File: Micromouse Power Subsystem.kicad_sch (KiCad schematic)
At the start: 3 parts, among them J2 Conn_02x16_Odd_Even, U1 INA219AxD

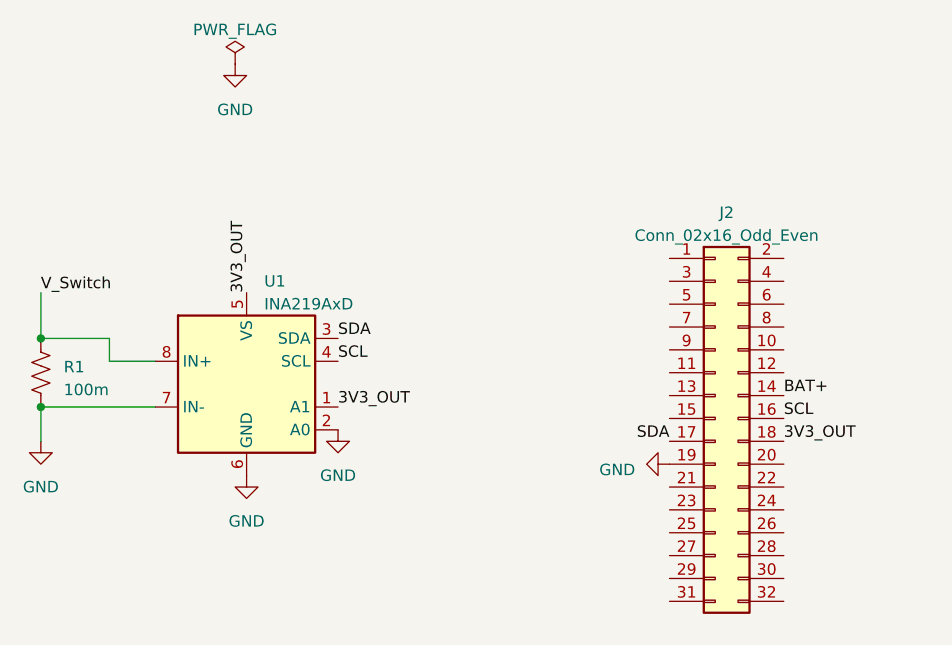
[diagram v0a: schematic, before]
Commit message: Added net labels for the 32 pin header
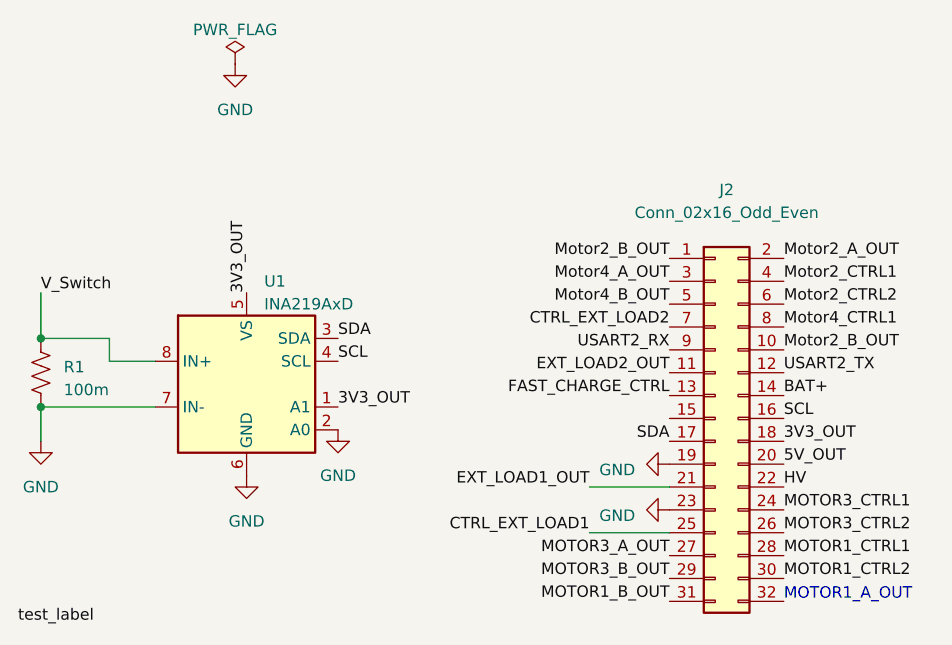
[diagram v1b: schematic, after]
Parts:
- R1: footprint (none) -> Resistor_SMD:R_Shunt_Ohmite_LVK12
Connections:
- net GND: now also J2.23 (Pin_23)
- net Motor2_B_OUT: now reaches J2.1 (Pin_1)
- net Motor2_B_OUT: now also J2.10 (Pin_10)
- net EXT_LOAD2_OUT: now reaches J2.11 (Pin_11)
- net USART2_TX: now reaches J2.12 (Pin_12)
- net FAST_CHARGE_CTRL: now reaches J2.13 (Pin_13)
- net Motor2_A_OUT: now reaches J2.2 (Pin_2)
- net 5V_OUT: now reaches J2.20 (Pin_20)
- net EXT_LOAD1_OUT: now reaches J2.21 (Pin_21)
- net HV: now reaches J2.22 (Pin_22)
- net MOTOR3_CTRL1: now reaches J2.24 (Pin_24)
- net CTRL_EXT_LOAD1: now reaches J2.25 (Pin_25)
- net MOTOR3_CTRL2: now reaches J2.26 (Pin_26)
- net MOTOR3_A_OUT: now reaches J2.27 (Pin_27)
- net MOTOR1_CTRL1: now reaches J2.28 (Pin_28)
- net MOTOR3_B_OUT: now reaches J2.29 (Pin_29)
- net Motor4_A_OUT: now reaches J2.3 (Pin_3)
- net MOTOR1_CTRL2: now reaches J2.30 (Pin_30)
- net MOTOR1_B_OUT: now reaches J2.31 (Pin_31)
- net Motor2_CTRL1: now reaches J2.4 (Pin_4)
- net Motor4_B_OUT: now reaches J2.5 (Pin_5)
- net Motor2_CTRL2: now reaches J2.6 (Pin_6)
- net CTRL_EXT_LOAD2: now reaches J2.7 (Pin_7)
- net Motor4_CTRL1: now reaches J2.8 (Pin_8)
- net USART2_RX: now reaches J2.9 (Pin_9)
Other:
- note added: "MOTOR1_A_OUT"
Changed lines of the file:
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@@
+    (stroke (width 0) (type default))
+  )
+  (wire (pts (xy 107.95 110.49) (xy 116.84 110.49))
     (stroke (width 0) (type default))
   )
@@
     (stroke (width 0) (type default))
   )
+  (wire (pts (xy 107.95 105.41) (xy 116.84 105.41))
+    (stroke (width 0) (type default))
+  )
   (wire (pts (xy 46.99 96.52) (xy 46.99 100.33))
     (stroke (width 0) (type default))
@@
     (stroke (width 0) (type default))
   )
+  (text "MOTOR1_A_OUT" (at 129.54 118.11 0)
+    (effects (font (size 1.27 1.27)) (justify left bottom))
+  )
   (label "3V3_OUT" (at 69.85 83.82 90) (fields_autoplaced)
     (effects (font (size 1.27 1.27)) (justify left bottom))
   )
+  (label "CTRL_EXT_LOAD2" (at 116.84 87.63 180) (fields_autoplaced)
+    (effects (font (size 1.27 1.27)) (justify right bottom))
+  )
+  (label "USART2_TX" (at 129.54 92.71 0) (fields_autoplaced)
+    (effects (font (size 1.27 1.27)) (justify left bottom))
+  )
+  (label "EXT_LOAD1_OUT" (at 107.95 105.41 180) (fields_autoplaced)
+    (effects (font (size 1.27 1.27)) (justify right bottom))
+  )
+  (label "MOTOR3_CTRL2" (at 129.54 110.49 0) (fields_autoplaced)
+    (effects (font (size 1.27 1.27)) (justify left bottom))
+  )
+  (label "EXT_LOAD2_OUT" (at 116.84 92.71 180) (fields_autoplaced)
+    (effects (font (size 1.27 1.27)) (justify right bottom))
+  )
+  (label "MOTOR1_CTRL1" (at 129.54 113.03 0) (fields_autoplaced)
+    (effects (font (size 1.27 1.27)) (justify left bottom))
+  )
+  (label "Motor2_CTRL1" (at 129.54 82.55 0) (fields_autoplaced)
+    (effects (font (size 1.27 1.27)) (justify left bottom))
+  )
+  (label "Motor4_A_OUT" (at 116.84 82.55 180) (fields_autoplaced)
+    (effects (font (size 1.27 1.27)) (justify right bottom))
+  )
+  (label "MOTOR3_CTRL1" (at 129.54 107.95 0) (fields_autoplaced)
+    (effects (font (size 1.27 1.27)) (justify left bottom))
+  )
+  (label "Motor2_A_OUT" (at 129.54 80.01 0) (fields_autoplaced)
+    (effects (font (size 1.27 1.27)) (justify left bottom))
+  )
+  (label "Motor2_CTRL2" (at 129.54 85.09 0) (fields_autoplaced)
+    (effects (font (size 1.27 1.27)) (justify left bottom))
+  )
   (label "V_Switch" (at 46.99 83.82 0) (fields_autoplaced)
     (effects (font (size 1.27 1.27)) (justify left bottom))
   )
+  (label "Motor4_CTRL1" (at 129.54 87.63 0) (fields_autoplaced)
+    (effects (font (size 1.27 1.27)) (justify left bottom))
+  )
+  (label "HV" (at 129.54 105.41 0) (fields_autoplaced)
+    (effects (font (size 1.27 1.27)) (justify left bottom))
+  )
+  (label "Motor2_B_OUT" (at 129.54 90.17 0) (fields_autoplaced)
+    (effects (font (size 1.27 1.27)) (justify left bottom))
+  )
   (label "3V3_OUT" (at 129.54 100.33 0) (fields_autoplaced)
     (effects (font (size 1.27 1.27)) (justify left bottom))
   )
+  (label "Motor4_B_OUT" (at 116.84 85.09 180) (fields_autoplaced)
+    (effects (font (size 1.27 1.27)) (justify right bottom))
+  )
+  (label "FAST_CHARGE_CTRL" (at 116.84 95.25 180) (fields_autoplaced)
+    (effects (font (size 1.27 1.27)) (justify right bottom))
+  )
+  (label "5V_OUT" (at 129.54 102.87 0) (fields_autoplaced)
+    (effects (font (size 1.27 1.27)) (justify left bottom))
+  )
+  (label "MOTOR1_CTRL2" (at 129.54 115.57 0) (fields_autoplaced)
+    (effects (font (size 1.27 1.27)) (justify left bottom))
+  )
   (label "SCL" (at 129.54 97.79 0) (fields_autoplaced)
     (effects (font (size 1.27 1.27)) (justify left bottom))
   )
+  (label "Motor2_B_OUT" (at 116.84 80.01 180) (fields_autoplaced)
+    (effects (font (size 1.27 1.27)) (justify right bottom))
+  )
+  (label "CTRL_EXT_LOAD1" (at 107.95 110.49 180) (fields_autoplaced)
+    (effects (font (size 1.27 1.27)) (justify right bottom))
+  )
   (label "BAT+" (at 129.54 95.25 0) (fields_autoplaced)
     (effects (font (size 1.27 1.27)) (justify left bottom))
   )
+  (label "test_label" (at 44.45 120.65 0) (fields_autoplaced)
+    (effects (font (size 1.27 1.27)) (justify left bottom))
+  )
+  (label "MOTOR3_A_OUT" (at 116.84 113.03 180) (fields_autoplaced)
+    (effects (font (size 1.27 1.27)) (justify right bottom))
+  )
+  (label "USART2_RX" (at 116.84 90.17 180) (fields_autoplaced)
+    (effects (font (size 1.27 1.27)) (justify right bottom))
+  )
   (label "3V3_OUT" (at 80.01 96.52 0) (fields_autoplaced)
     (effects (font (size 1.27 1.27)) (justify left bottom))
@@
   (label "SCL" (at 80.01 91.44 0) (fields_autoplaced)
     (effects (font (size 1.27 1.27)) (justify left bottom))
+  )
+  (label "MOTOR3_B_OUT" (at 116.84 115.57 180) (fields_autoplaced)
+    (effects (font (size 1.27 1.27)) (justify right bottom))
+  )
+  (label "MOTOR1_B_OUT" (at 116.84 118.11 180) (fields_autoplaced)
+    (effects (font (size 1.27 1.27)) (justify right bottom))
   )
   (label "SDA" (at 116.84 100.33 180) (fields_autoplaced)
@@
     )
   )
+  (symbol (lib_id "power:GND") (at 116.84 107.95 270) (unit 1)
+    (in_bom yes) (on_board yes) (dnp no) (fields_autoplaced)
+    (property "Reference" "#PWR06" (at 110.49 107.95 0)
+      (effects (font (size 1.27 1.27)) hide)
+    )
+    (property "Value" "GND" (at 113.03 108.585 90)
+      (effects (font (size 1.27 1.27)) (justify right))
+    )
+    (property "Footprint" "" (at 116.84 107.95 0)
+      (effects (font (size 1.27 1.27)) hide)
+    )
+    (property "Datasheet" "" (at 116.84 107.95 0)
+      (effects (font (size 1.27 1.27)) hide)
+    )
+    (pin "1")
+    (instances
+      (project "Micromouse Power Subsystem"
+        (path "/c31c9b5f-16c8-4039-9f8b-b05613c282c9"
+          (reference "#PWR06") (unit 1)
+        )
+      )
+    )
+  )
   (symbol (lib_id "Connector_Generic:Conn_02x16_Odd_Even") (at 121.92 97.79 0) (unit 1)
-    (in_bom yes) (on_board yes) (dnp no) (fields_autoplaced)
-    (property "Reference" "J2" (at 123.19 74.93 0)
+    (in_bom yes) (on_board yes) (dnp no)
+    (property "Reference" "J2" (at 123.19 72.39 0)
       (effects (font (size 1.27 1.27)))
     )
-    (property "Value" "Conn_02x16_Odd_Even" (at 123.19 77.47 0)
+    (property "Value" "Conn_02x16_Odd_Even" (at 123.19 74.93 0)
       (effects (font (size 1.27 1.27)))
     )
@@
       (effects (font (size 1.27 1.27)) (justify right))
     )
-    (property "Footprint" "" (at 45.974 92.456 90)
-      (effects (font (size 1.27 1.27)) hide)
-    )
+    (property "Footprint" "Resistor_SMD:R_Shunt_Ohmite_LVK12" (at 45.974 92.456 90)
+      (effects (font (size 1.27 1.27)) hide)
+    )
